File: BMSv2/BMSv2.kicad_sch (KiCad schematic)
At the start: 120 parts, among them J2 Conn_01x04_Socket, J3 Conn_01x02_Pin, Q1 AO3401A, SW1 SW_BOOT0, U1 STM32F405RGTx, U2 MCP2561-E-SN, U4 MP2332H, U5 AMS1117-3.3

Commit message: Add files via upload
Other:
- note added: "Balanser"
- note added: "High_speed_clock"
- note added: "Led_status"
- note added: "NTC_Temp_Controll"
- note added: "Overvoltage Protection"
- note added: "Power_connector"
- note added: "Programator"
- note added: "WCS1500_current_sensor"
- moved on the sheet: C13, C14, C15, C16, C17, C18, C19, C20, C21, C22, C23, C24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

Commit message: Add files via upload
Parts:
- added J4: Conn_01x02_Pin, Connector_Molex:Molex_KK-254_AE-6410-02A_1x02_P2.54mm_Vertical, symbol Connector:Conn_01x02_Pin
- added J5: Conn_01x03_Pin, Connector_PinHeader_2.54mm:PinHeader_1x03_P2.54mm_Vertical, symbol Connector:Conn_01x03_Pin
- J3: footprint Connector_JST:JST_XA_S02B-XASK-1_1x02_P2.50mm_Horizontal -> Connector_Molex:Molex_KK-254_AE-6410-02A_1x02_P2.54mm_Vertical
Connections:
- net CAN1+: now also J4.1 (Pin_1)
- net CAN1-: now also J4.2 (Pin_2)
- net CL1_DCH: now also U1.50 (PA15); no longer U1.27 (PB1)
- net CL2_DCH: now also U1.51 (PC10); no longer U1.28 (PB2)
- net CL3_DCH: now also U1.52 (PC11); no longer U1.29 (PB10)
- net CL4_DCH: now also U1.53 (PC12); no longer U1.30 (PB11)
- net GND: now also J5.3 (Pin_3)
- net Temp1: now also U1.23 (PA7); no longer U1.8 (PC0)
- net Temp2: now also U1.22 (PA6); no longer U1.9 (PC1)
- net Temp3: now also U1.21 (PA5); no longer U1.10 (PC2)
- net Temp4: now also U1.20 (PA4); no longer U1.11 (PC3)
- net UART_RX: now reaches U1.42 (PA9)
- net UART_RX: now also J5.1 (Pin_1)
- net UART_TX: now reaches U1.43 (PA10)
- net UART_TX: now also J5.2 (Pin_2)
- no-connect marks 26 -> 24
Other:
- note added: "Can_connector"
- note added: "UART"
- moved on the sheet: C13, D1, F1, FB1, Q1

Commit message: Add files via upload
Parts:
- added H1, H2, H3, H4: MountingHole, MountingHole:MountingHole_2.2mm_M2, symbol Mechanical:MountingHole
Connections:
- net +3V3 is gone; now on net +3.3V: J2.3 (Pin_3), R1.1, R2.1, R3.1, R4.1
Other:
- note added: "Mounting"
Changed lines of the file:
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@@
     (stroke (width 0) (type default))
   )
+  (polyline (pts (xy 208.407 142.748) (xy 208.407 204.343))
+    (stroke (width 0) (type default))
+  )
   (wire (pts (xy 363.22 120.015) (xy 363.22 121.285))
     (stroke (width 0) (type default))
@@
     (effects (font (size 1.27 1.27)) (justify left bottom))
   )
+  (text "Mounting" (at 220.091 154.559 0)
+    (effects (font (size 1.27 1.27)) (justify left bottom))
+  )
   (text "Balanser" (at 345.821 17.907 0)
     (effects (font (size 1.27 1.27)) (justify left bottom))
@@
     )
   )
-  (symbol (lib_id "power:+3V3") (at 272.669 30.099 0) (unit 1)
-    (in_bom yes) (on_board yes) (dnp no) (fields_autoplaced)
-    (property "Reference" "#PWR01" (at 272.669 33.909 0)
-      (effects (font (size 1.27 1.27)) hide)
-    )
-    (property "Value" "+3V3" (at 272.669 25.019 0)
-      (effects (font (size 1.27 1.27)))
-    )
-    (property "Footprint" "" (at 272.669 30.099 0)
-      (effects (font (size 1.27 1.27)) hide)
-    )
-    (property "Datasheet" "" (at 272.669 30.099 0)
-      (effects (font (size 1.27 1.27)) hide)
-    )
-    (pin "1")
-    (instances
-      (project "BMSv2"
-        (path "/a5c08c1c-7045-4a3a-8914-115fdd89801e"
-          (reference "#PWR01") (unit 1)
-        )
-      )
-    )
-  )
   (symbol (lib_id "Device:C") (at 38.9135 121.1065 0) (unit 1)
     (in_bom yes) (on_board yes) (dnp no)
@@
     )
   )
+  (symbol (lib_id "Mechanical:MountingHole") (at 217.932 167.259 0) (unit 1)
+    (in_bom yes) (on_board yes) (dnp no) (fields_autoplaced)
+    (property "Reference" "H2" (at 220.853 165.989 0)
+      (effects (font (size 1.27 1.27)) (justify left))
+    )
+    (property "Value" "MountingHole" (at 220.853 168.529 0)
+      (effects (font (size 1.27 1.27)) (justify left))
+    )
+    (property "Footprint" "MountingHole:MountingHole_2.2mm_M2" (at 217.932 167.259 0)
+      (effects (font (size 1.27 1.27)) hide)
+    )
+    (property "Datasheet" "~" (at 217.932 167.259 0)
+      (effects (font (size 1.27 1.27)) hide)
+    )
+    (instances
+      (project "BMSv2"
+        (path "/a5c08c1c-7045-4a3a-8914-115fdd89801e"
+          (reference "H2") (unit 1)
+        )
+      )
+    )
+  )
   (symbol (lib_id "Device:C") (at 30.6585 121.1065 0) (unit 1)
     (in_bom yes) (on_board yes) (dnp no)
@@
     )
   )
+  (symbol (lib_id "Mechanical:MountingHole") (at 217.932 161.29 0) (unit 1)
+    (in_bom yes) (on_board yes) (dnp no) (fields_autoplaced)
+    (property "Reference" "H1" (at 220.853 160.02 0)
+      (effects (font (size 1.27 1.27)) (justify left))
+    )
+    (property "Value" "MountingHole" (at 220.853 162.56 0)
+      (effects (font (size 1.27 1.27)) (justify left))
+    )
+    (property "Footprint" "MountingHole:MountingHole_2.2mm_M2" (at 217.932 161.29 0)
+      (effects (font (size 1.27 1.27)) hide)
+    )
+    (property "Datasheet" "~" (at 217.932 161.29 0)
+      (effects (font (size 1.27 1.27)) hide)
+    )
+    (instances
+      (project "BMSv2"
+        (path "/a5c08c1c-7045-4a3a-8914-115fdd89801e"
+          (reference "H1") (unit 1)
+        )
+      )
+    )
+  )
   (symbol (lib_id "Device:R_Small") (at 39.37 177.8 0) (unit 1)
     (in_bom yes) (on_board yes) (dnp no) (fields_autoplaced)
@@
     )
   )
+  (symbol (lib_id "power:+3.3V") (at 272.669 30.099 0) (unit 1)
+    (in_bom yes) (on_board yes) (dnp no) (fields_autoplaced)
+    (property "Reference" "#PWR01" (at 272.669 33.909 0)
+      (effects (font (size 1.27 1.27)) hide)
+    )
+    (property "Value" "+3.3V" (at 272.669 25.527 0)
+      (effects (font (size 1.27 1.27)))
+    )
+    (property "Footprint" "" (at 272.669 30.099 0)
+      (effects (font (size 1.27 1.27)) hide)
+    )
+    (property "Datasheet" "" (at 272.669 30.099 0)
+      (effects (font (size 1.27 1.27)) hide)
+    )
+    (pin "1")
+    (instances
+      (project "BMSv2"
+        (path "/a5c08c1c-7045-4a3a-8914-115fdd89801e"
+          (reference "#PWR01") (unit 1)
+        )
+      )
+    )
+  )
   (symbol (lib_id "power:+3.3V") (at 376.936 163.195 0) (unit 1)
     (in_bom yes) (on_board yes) (dnp no)
@@
     )
   )
+  (symbol (lib_id "Mechanical:MountingHole") (at 217.932 179.705 0) (unit 1)
+    (in_bom yes) (on_board yes) (dnp no) (fields_autoplaced)
+    (property "Reference" "H4" (at 220.853 178.435 0)
+      (effects (font (size 1.27 1.27)) (justify left))
+    )
+    (property "Value" "MountingHole" (at 220.853 180.975 0)
+      (effects (font (size 1.27 1.27)) (justify left))
+    )
+    (property "Footprint" "MountingHole:MountingHole_2.2mm_M2" (at 217.932 179.705 0)
+      (effects (font (size 1.27 1.27)) hide)
+    )
+    (property "Datasheet" "~" (at 217.932 179.705 0)
+      (effects (font (size 1.27 1.27)) hide)
+    )
+    (instances
+      (project "BMSv2"
+        (path "/a5c08c1c-7045-4a3a-8914-115fdd89801e"
+          (reference "H4") (unit 1)
+        )
+      )
+    )
+  )
   (symbol (lib_id "Device:C") (at 37.0085 34.7465 0) (unit 1)
     (in_bom yes) (on_board yes) (dnp no)
@@
     )
   )
+  (symbol (lib_id "power:+3.3V") (at 141.224 86.106 90) (unit 1)
+    (in_bom yes) (on_board yes) (dnp no) (fields_autoplaced)
+    (property "Reference" "#PWR049" (at 145.034 86.106 0)
+      (effects (font (size 1.27 1.27)) hide)
+    )
+    (property "Value" "+3.3V" (at 137.795 86.106 90)
+      (effects (font (size 1.27 1.27)) (justify left))
+    )
+    (property "Footprint" "" (at 141.224 86.106 0)
+      (effects (font (size 1.27 1.27)) hide)
+    )
+    (property "Datasheet" "" (at 141.224 86.106 0)
+      (effects (font (size 1.27 1.27)) hide)
+    )
+    (pin "1")
+    (instances
+      (project "BMSv2"
+        (path "/a5c08c1c-7045-4a3a-8914-115fdd89801e"
+          (reference "#PWR049") (unit 1)
+        )
+      )
+    )
+  )
   (symbol (lib_id "Device:LED") (at 267.589 114.681 270) (mirror x) (unit 1)
     (in_bom yes) (on_board yes) (dnp no) (fields_autoplaced)
@@
     )
   )
+  (symbol (lib_id "Mechanical:MountingHole") (at 218.059 173.482 0) (unit 1)
+    (in_bom yes) (on_board yes) (dnp no) (fields_autoplaced)
+    (property "Reference" "H3" (at 220.98 172.212 0)
+      (effects (font (size 1.27 1.27)) (justify left))
+    )
+    (property "Value" "MountingHole" (at 220.98 174.752 0)
+      (effects (font (size 1.27 1.27)) (justify left))
+    )
+    (property "Footprint" "MountingHole:MountingHole_2.2mm_M2" (at 218.059 173.482 0)
+      (effects (font (size 1.27 1.27)) hide)
+    )
+    (property "Datasheet" "~" (at 218.059 173.482 0)
+      (effects (font (size 1.27 1.27)) hide)
+    )
+    (instances
+      (project "BMSv2"
+        (path "/a5c08c1c-7045-4a3a-8914-115fdd89801e"
+          (reference "H3") (unit 1)
+        )
+      )
+    )
+  )
   (symbol (lib_id "power:GND") (at 16.0535 56.3365 0) (unit 1)
     (in_bom yes) (on_board yes) (dnp no) (fields_autoplaced)
@@
         )
       )
-    )
-  )
-  (symbol (lib_id "power:+3V3") (at 141.224 86.106 90) (unit 1)
-    (in_bom yes) (on_board yes) (dnp no) (fields_autoplaced)
-    (property "Reference" "#PWR049" (at 145.034 86.106 0)
-      (effects (font (size 1.27 1.27)) hide)
-    )
-    (property "Value" "+3V3" (at 137.1346 86.106 90)
-      (effects (font (size 1.27 1.27)) (justify left))
-    )
-    (property "Footprint" "" (at 141.224 86.106 0)
-      (effects (font (size 1.27 1.27)) hide)
-    )
-    (property "Datasheet" "" (at 141.224 86.106 0)
-      (effects (font (size 1.27 1.27)) hide)
-    )
-    (pin "1")
-    (instances
-      (project "BMSv2"
-        (path "/a5c08c1c-7045-4a3a-8914-115fdd89801e"
-          (reference "#PWR049") (unit 1)
-        )
-      )

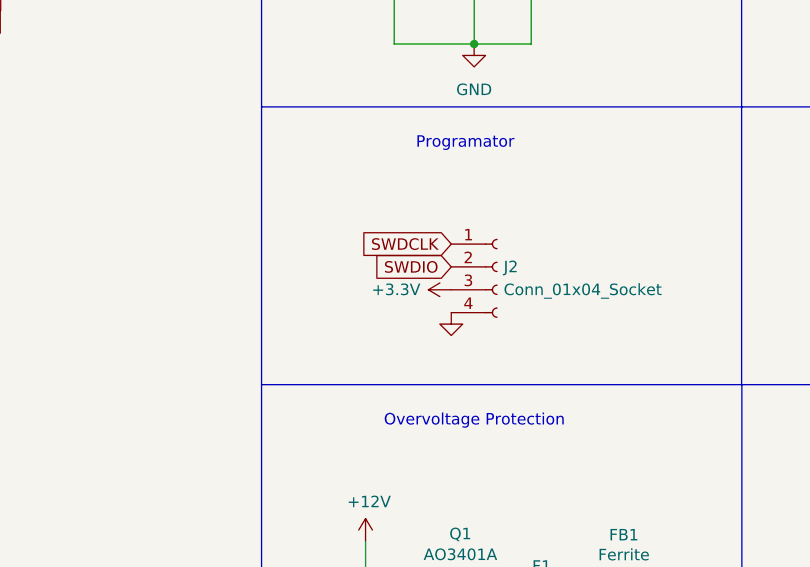
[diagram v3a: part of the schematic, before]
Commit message: Added for Front flayer
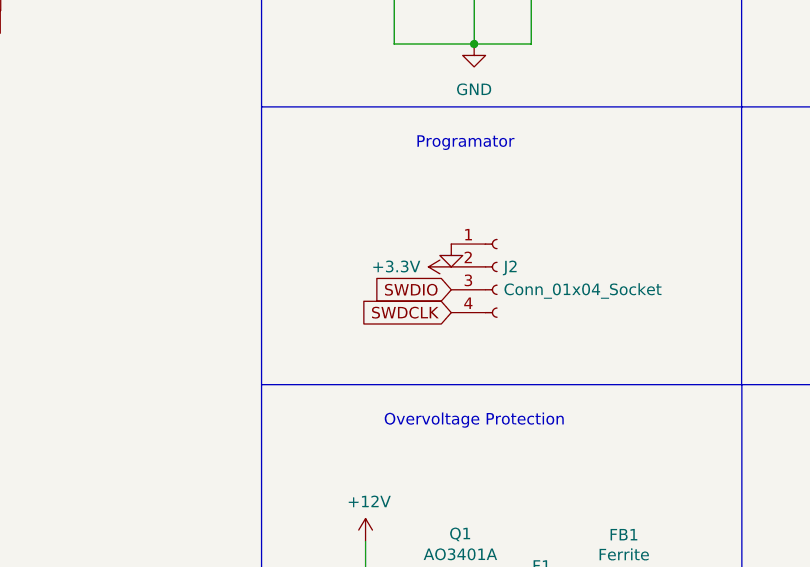
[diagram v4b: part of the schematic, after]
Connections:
- net +3.3V: now also J2.2 (Pin_2); no longer J2.3 (Pin_3)
- net GND: now also J2.1 (Pin_1); no longer J2.4 (Pin_4)
- net SWDCLK: now also J2.4 (Pin_4); no longer J2.1 (Pin_1)
- net SWDIO: now also J2.3 (Pin_3); no longer J2.2 (Pin_2)
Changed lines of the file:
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@@
     )
   )
-  (global_label "SWDIO" (shape input) (at 141.224 83.566 180) (fields_autoplaced)
-    (effects (font (size 1.27 1.27)) (justify right))
-    (property "Intersheetrefs" "${INTERSHEET_REFS}" (at 132.3726 83.566 0)
-      (effects (font (size 1.27 1.27)) (justify right) hide)
-    )
-  )
   (global_label "CELL3_M" (shape input) (at 94.742 182.372 0) (fields_autoplaced)
     (effects (font (size 1.27 1.27)) (justify left))
@@
     )
   )
-  (global_label "SWDCLK" (shape input) (at 141.224 81.026 180) (fields_autoplaced)
-    (effects (font (size 1.27 1.27)) (justify right))
-    (property "Intersheetrefs" "${INTERSHEET_REFS}" (at 130.7398 81.026 0)
-      (effects (font (size 1.27 1.27)) (justify right) hide)
-    )
-  )
   (global_label "CAN1-" (shape input) (at 231.5718 47.7774 0) (fields_autoplaced)
     (effects (font (size 1.27 1.27)) (justify left))
@@
     )
   )
+  (global_label "SWDCLK" (shape input) (at 141.224 88.646 180) (fields_autoplaced)
+    (effects (font (size 1.27 1.27)) (justify right))
+    (property "Intersheetrefs" "${INTERSHEET_REFS}" (at 130.7398 88.646 0)
+      (effects (font (size 1.27 1.27)) (justify right) hide)
+    )
+  )
   (global_label "CELL2" (shape input) (at 127.762 156.21 90) (fields_autoplaced)
     (effects (font (size 1.27 1.27)) (justify left))
@@
     )
   )
+  (global_label "SWDIO" (shape input) (at 141.224 86.106 180) (fields_autoplaced)
+    (effects (font (size 1.27 1.27)) (justify right))
+    (property "Intersheetrefs" "${INTERSHEET_REFS}" (at 132.3726 86.106 0)
+      (effects (font (size 1.27 1.27)) (justify right) hide)
+    )
+  )
   (global_label "CELL1_M_TRIG" (shape input) (at 147.574 176.53 90) (fields_autoplaced)
     (effects (font (size 1.27 1.27)) (justify left))
@@
     )
   )
-  (symbol (lib_id "power:GND") (at 141.224 88.646 0) (unit 1)
-    (in_bom yes) (on_board yes) (dnp no) (fields_autoplaced)
-    (property "Reference" "#PWR050" (at 141.224 94.996 0)
-      (effects (font (size 1.27 1.27)) hide)
-    )
-    (property "Value" "GND" (at 141.224 93.726 0)
-      (effects (font (size 1.27 1.27)) hide)
-    )
-    (property "Footprint" "" (at 141.224 88.646 0)
-      (effects (font (size 1.27 1.27)) hide)
-    )
-    (property "Datasheet" "" (at 141.224 88.646 0)
-      (effects (font (size 1.27 1.27)) hide)
-    )
-    (pin "1")
-    (instances
-      (project "BMSv2"
-        (path "/a5c08c1c-7045-4a3a-8914-115fdd89801e"
-          (reference "#PWR050") (unit 1)
-        )
-      )
-    )
-  )
   (symbol (lib_id "Device:R") (at 325.12 74.295 90) (unit 1)
     (in_bom yes) (on_board yes) (dnp no)
@@
     )
   )
+  (symbol (lib_id "power:GND") (at 141.224 81.026 0) (unit 1)
+    (in_bom yes) (on_board yes) (dnp no) (fields_autoplaced)
+    (property "Reference" "#PWR050" (at 141.224 87.376 0)
+      (effects (font (size 1.27 1.27)) hide)
+    )
+    (property "Value" "GND" (at 141.224 86.106 0)
+      (effects (font (size 1.27 1.27)) hide)
+    )
+    (property "Footprint" "" (at 141.224 81.026 0)
+      (effects (font (size 1.27 1.27)) hide)
+    )
+    (property "Datasheet" "" (at 141.224 81.026 0)
+      (effects (font (size 1.27 1.27)) hide)
+    )
+    (pin "1")
+    (instances
+      (project "BMSv2"
+        (path "/a5c08c1c-7045-4a3a-8914-115fdd89801e"
+          (reference "#PWR050") (unit 1)
+        )
+      )
+    )
+  )
   (symbol (lib_id "power:GND") (at 101.6 162.814 0) (unit 1)
     (in_bom yes) (on_board yes) (dnp no) (fields_autoplaced)
@@
     )
   )
+  (symbol (lib_id "power:+3.3V") (at 141.224 83.566 90) (unit 1)
+    (in_bom yes) (on_board yes) (dnp no) (fields_autoplaced)
+    (property "Reference" "#PWR049" (at 145.034 83.566 0)
+      (effects (font (size 1.27 1.27)) hide)
+    )
+    (property "Value" "+3.3V" (at 137.795 83.566 90)
+      (effects (font (size 1.27 1.27)) (justify left))
+    )
+    (property "Footprint" "" (at 141.224 83.566 0)
+      (effects (font (size 1.27 1.27)) hide)
+    )
+    (property "Datasheet" "" (at 141.224 83.566 0)
+      (effects (font (size 1.27 1.27)) hide)
+    )
+    (pin "1")
+    (instances
+      (project "BMSv2"
+        (path "/a5c08c1c-7045-4a3a-8914-115fdd89801e"
+          (reference "#PWR049") (unit 1)
+        )
+      )
+    )
+  )
   (symbol (lib_id "power:+5V") (at 357.886 163.195 0) (unit 1)
     (in_bom yes) (on_board yes) (dnp no) (fields_autoplaced)
@@
         )
       )
-    )
-  )
-  (symbol (lib_id "power:+3.3V") (at 141.224 86.106 90) (unit 1)
-    (in_bom yes) (on_board yes) (dnp no) (fields_autoplaced)
-    (property "Reference" "#PWR049" (at 145.034 86.106 0)
-      (effects (font (size 1.27 1.27)) hide)
-    )
-    (property "Value" "+3.3V" (at 137.795 86.106 90)
-      (effects (font (size 1.27 1.27)) (justify left))
-    )
-    (property "Footprint" "" (at 141.224 86.106 0)
-      (effects (font (size 1.27 1.27)) hide)
-    )
-    (property "Datasheet" "" (at 141.224 86.106 0)
-      (effects (font (size 1.27 1.27)) hide)
-    )
-    (pin "1")
-    (instances
-      (project "BMSv2"
-        (path "/a5c08c1c-7045-4a3a-8914-115fdd89801e"
-          (reference "#PWR049") (unit 1)
-        )
-      )

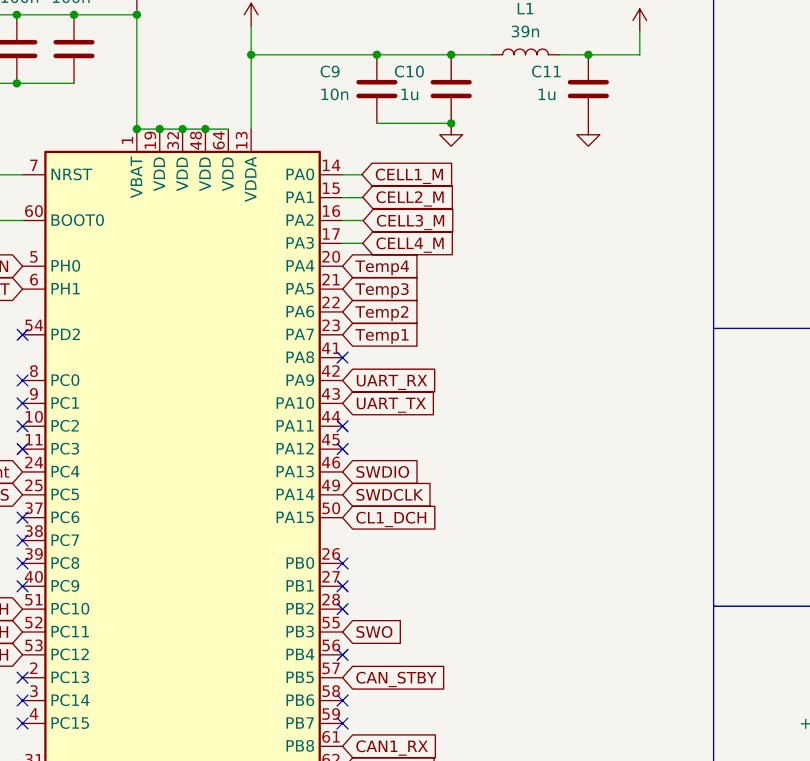
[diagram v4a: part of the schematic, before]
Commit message: Solving DRC Errors
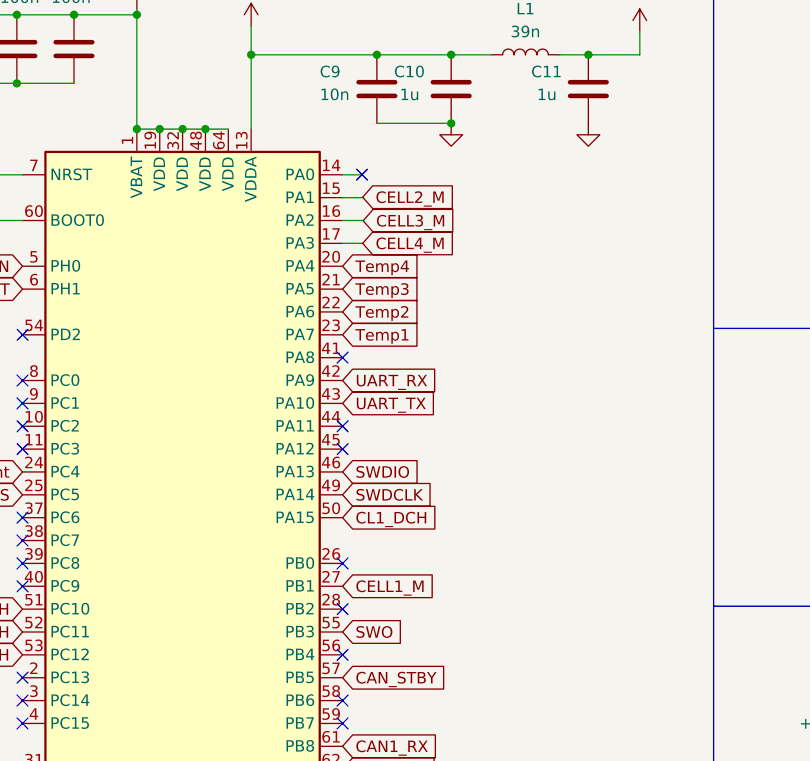
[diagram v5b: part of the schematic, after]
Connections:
- net CELL1_M: now also U1.27 (PB1); no longer U1.14 (PA0)
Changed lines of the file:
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@@
   (no_connect (at 43.3585 79.1965))
   (no_connect (at 43.3585 66.4965))
+  (no_connect (at 81.0768 48.701))
   (no_connect (at 43.3585 91.8965))
   (no_connect (at 78.9185 117.2965))
@@
   (no_connect (at 43.3585 107.1365))
   (no_connect (at 43.3585 71.5765))
-  (no_connect (at 78.9185 94.4365))
   (wire (pts (xy 201.295 25.527) (xy 201.295 26.797))
     (stroke (width 0) (type default))
@@
   (label "CAN1_RX" (at 192.913 42.672 180) (fields_autoplaced)
     (effects (font (size 1.27 1.27)) (justify right bottom))
-  )
-  (global_label "CELL1_M" (shape input) (at 81.0768 48.6918 0) (fields_autoplaced)
-    (effects (font (size 1.27 1.27)) (justify left))
-    (property "Intersheetrefs" "${INTERSHEET_REFS}" (at 92.1657 48.6918 0)
-      (effects (font (size 1.27 1.27)) (justify left) hide)
-    )
   )
   (global_label "CELL3_M" (shape input) (at 94.742 182.372 0) (fields_autoplaced)
@@
       (effects (font (size 1.27 1.27)) (justify left) hide)
     )
+  )
+  (global_label "CELL1_M" (shape input) (at 78.9185 94.4365 0) (fields_autoplaced)
+    (effects (font (size 1.27 1.27)) (justify left))
+    (property "Intersheetrefs" "${INTERSHEET_REFS}" (at 90.0074 94.4365 0)
+      (effects (font (size 1.27 1.27)) (justify left) hide)
+    )
